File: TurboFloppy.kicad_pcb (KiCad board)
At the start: 2 copper layers, 52.1 x 66.2 mm, 10 parts, among them CN1 EXPANSION_PORT, CN3 PIN_HEADER_32PIN, U1 8255, U2 GAL20V8

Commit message: Add pull-ups on all 8255 ports
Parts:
- added RN1: 10k, Resistor_THT:R_Array_SIP9, F.Cu at (149.9, 105.9)
- added RN2: 10k, Resistor_THT:R_Array_SIP9, F.Cu at (142.2, 83.1)
- added RN3: 10k, Resistor_THT:R_Array_SIP9, F.Cu at (149.9, 83.1)
- moved CN3 3.81 mm to (165.1, 72.9)
- moved H1 3.81 mm to (123.2, 69.8)
- moved H2 3.81 mm to (168.9, 69.8)
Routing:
- net /pb3: track 35.4 -> 72.4 mm
- net /pb7: track 30.8 -> 64.1 mm
- net /pb5: track 33.3 -> 66.7 mm
- net /pb6: track 27.5 -> 60.8 mm
- net /pc4: track 18.0 -> 39.1 mm
- net /pc6: track 18.0 -> 36.0 mm
- net /pc5: track 18.0 -> 36.0 mm
- net /pc7: track 18.8 -> 36.0 mm
- net +5V: track 97.4 -> 114.5 mm
- net /pa4: track 37.9 -> 45.7 mm
- net /pa6: track 28.5 -> 36.3 mm
- net /pa5: track 33.2 -> 41.0 mm
- net /pa7: track 29.7 -> 37.4 mm
- net /d1: track 32.6 -> 37.7 mm
- net /d0: track 33.4 -> 38.3 mm
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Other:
- board size 52.1 x 66.2 mm -> 52.1 x 70 mm

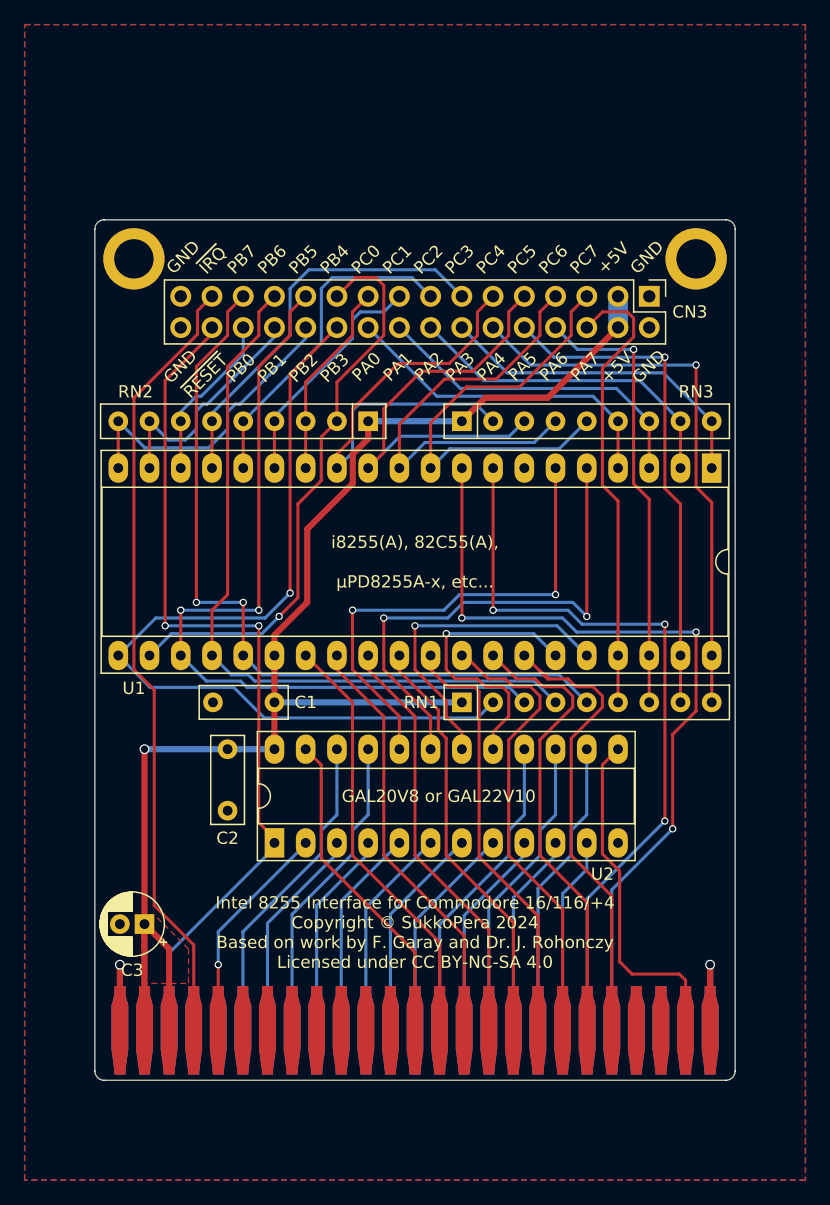
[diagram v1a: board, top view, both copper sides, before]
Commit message: Rework some tracks
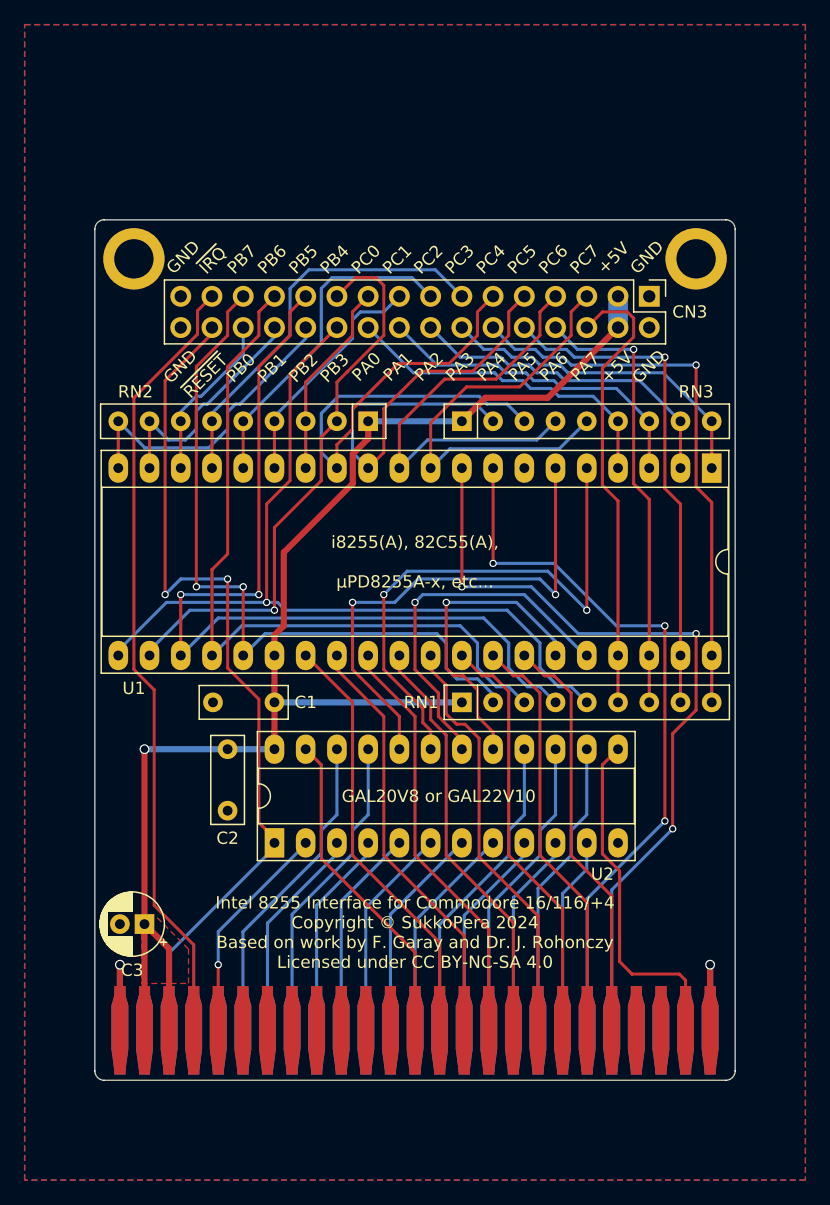
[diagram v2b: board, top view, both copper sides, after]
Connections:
- RN1 pad 2: /pb3 -> /pb7
- RN1 pad 3: /pb5 -> /pb6
- RN1 pad 4: /pb6 -> /pb5
- RN1 pad 5: /pb7 -> /pb3
- RN3 pad 2: /pc4 -> /pc5
- RN3 pad 3: /pc5 -> /pc4
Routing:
- net /pb5: track 66.7 -> 72.9 mm
- net /pc4: track 39.1 -> 44.6 mm
- net /pb7: track 64.1 -> 59.6 mm
- net /d0: track 38.3 -> 33.9 mm
- net /d1: track 37.7 -> 34.1 mm
- net /pc5: track 36.0 -> 39.2 mm
- net /~{wr8255}: track 26.6 -> 29.8 mm
- net /d2: track 37.5 -> 34.4 mm
- net /pb3: track 72.4 -> 69.4 mm
- net /~{rd8255}: track 41.8 -> 44.6 mm
- net /a1: track 61.6 -> 59.3 mm
- net /reset: track 23.5 -> 25.3 mm
- net /a0: track 66.9 -> 65.4 mm
- net /~{cs8255}: track 40.2 -> 41.6 mm
- net /d3: track 35.4 -> 34.5 mm
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
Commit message: Minor tweaks + Add URL
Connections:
- RN1 pad 5: /pb3 -> /pb4
- RN2 pad 2: /pb4 -> /pb3
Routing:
- net /pb4: track 46.7 -> 69.5 mm
- net /pb3: track 69.4 -> 50.6 mm
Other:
- board text added: "Intel 8255 Interface for Commodore 16/116/+4 Copyright © SukkoPera 2024 Based on work by F. Garay and Dr. J. Rohonczy Licensed under CC BY-NC-SA 4.0 github.com/SukkoPera/Plus4i8255"
- board text removed: "Intel 8255 Interface for Commodore 16/116/+4 Copyright © SukkoPera 2024 Based on work by F. Garay and Dr. J. Rohonczy Licensed under CC BY-NC-SA 4.0"
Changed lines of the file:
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@@
 			(layers "*.Cu" "*.Mask")
 			(remove_unused_layers no)
-			(net 60 "/pb3")
+			(net 46 "/pb4")
 			(pinfunction "R4")
 			(pintype "passive")
@@
 			(layers "*.Cu" "*.Mask")
 			(remove_unused_layers no)
-			(net 46 "/pb4")
+			(net 60 "/pb3")
 			(pinfunction "R1")
 			(pintype "passive")
@@
 		(tags "THT DIP DIL PDIP 2.54mm 7.62mm 300mil Socket LongPads")
 		(property "Reference" "U2"
-			(at -2.54 26.67 180)
+			(at 7.62 30.734 180)
 			(layer "F.SilkS")
 			(effects
@@
 		)
 	)
-	(gr_text "Intel 8255 Interface for Commodore 16/116/+4\nCopyright © SukkoPera 2024\nBased on work by F. Garay and Dr. J. Rohonczy\nLicensed under CC BY-NC-SA 4.0"
+	(gr_text "Intel 8255 Interface for Commodore 16/116/+4\nCopyright © SukkoPera 2024\nBased on work by F. Garay and Dr. J. Rohonczy\nLicensed under CC BY-NC-SA 4.0\ngithub.com/SukkoPera/Plus4i8255"
 		(at 146.05 127.635 0)
 		(layer "F.SilkS")
@@
 	)
 	(segment
-		(start 140.5255 79.0575)
-		(end 143.51 76.073)
+		(start 133.985 89.789)
+		(end 135.89 87.884)
 		(width 0.25)
 		(layer "F.Cu")
@@
 	)
 	(segment
-		(start 138.43 84.328)
-		(end 138.43 87.884)
+		(start 135.89 78.613)
+		(end 138.43 76.073)
 		(width 0.25)
 		(layer "F.Cu")
@@
 	)
 	(segment
-		(start 143.51 72.009)
-		(end 142.875 71.374)
+		(start 138.43 76.073)
+		(end 138.43 74.168)
 		(width 0.25)
 		(layer "F.Cu")
@@
 	)
 	(segment
-		(start 142.875 71.374)
-		(end 141.224 71.374)
+		(start 135.89 87.884)
+		(end 135.89 78.613)
 		(width 0.25)
 		(layer "F.Cu")
@@
 	)
 	(segment
-		(start 139.7 79.883)
-		(end 140.5255 79.0575)
+		(start 138.43 74.168)
+		(end 139.7 72.898)
 		(width 0.25)
 		(layer "F.Cu")
@@
 	)
 	(segment
-		(start 134.62 91.694)
-		(end 134.62 98.425)
+		(start 133.985 98.425)
+		(end 133.985 89.789)
 		(width 0.25)
 		(layer "F.Cu")
 		(net 46)
 	)
+	(via
+		(at 133.985 98.425)
+		(size 0.6)
+		(drill 0.4)
+		(layers "F.Cu" "B.Cu")
+		(net 46)
+	)
 	(segment
-		(start 138.43 87.884)
-		(end 134.62 91.694)
+		(start 124.46 102.108)
+		(end 124.46 101.708)
 		(width 0.25)
-		(layer "F.Cu")
+		(layer "B.Cu")
 		(net 46)
 	)
 	(segment
-		(start 139.7 83.058)
-		(end 139.7 79.883)
+		(start 156.21 103.124)
+		(end 157.734 104.648)
 		(width 0.25)
-		(layer "F.Cu")
+		(layer "B.Cu")
 		(net 46)
 	)
 	(segment
-		(start 143.51 76.073)
-		(end 143.51 72.009)
+		(start 153.543 98.425)
+		(end 156.21 101.092)
 		(width 0.25)
-		(layer "F.Cu")
+		(layer "B.Cu")
 		(net 46)
 	)
 	(segment
-		(start 139.7 83.058)
-		(end 138.43 84.328)
+		(start 156.21 101.092)
+		(end 156.21 103.124)
 		(width 0.25)
-		(layer "F.Cu")
+		(layer "B.Cu")
 		(net 46)
 	)
 	(segment
-		(start 141.224 71.374)
-		(end 139.7 72.898)
+		(start 157.734 104.648)
+		(end 158.75 104.648)
 		(width 0.25)
-		(layer "F.Cu")
+		(layer "B.Cu")
 		(net 46)
 	)
-	(via
-		(at 134.62 98.425)
-		(size 0.6)
-		(drill 0.4)
-		(layers "F.Cu" "B.Cu")
+	(segment
+		(start 127.743 98.425)
+		(end 133.985 98.425)
+		(width 0.25)
+		(layer "B.Cu")
 		(net 46)
 	)
 	(segment
-		(start 124.46 101.708)
-		(end 127.743 98.425)
+		(start 133.985 98.425)
+		(end 153.543 98.425)
 		(width 0.25)
 		(layer "B.Cu")
@@
 	)
 	(segment
-		(start 124.46 102.108)
-		(end 124.46 101.708)
+		(start 124.46 101.708)
+		(end 127.743 98.425)
 		(width 0.25)
 		(layer "B.Cu")
@@
 	)
 	(segment
-		(start 127.743 98.425)
-		(end 134.62 98.425)
+		(start 158.75 104.648)
+		(end 160.02 105.918)
 		(width 0.25)
 		(layer "B.Cu")
@@
 	)
 	(segment
-		(start 133.985 97.79)
-		(end 133.985 89.789)
+		(start 138.43 84.328)
+		(end 138.43 87.884)
 		(width 0.25)
 		(layer "F.Cu")
@@
 	)
 	(segment
-		(start 133.985 89.789)
-		(end 135.89 87.884)
+		(start 139.7 83.058)
+		(end 139.7 79.883)
 		(width 0.25)
 		(layer "F.Cu")
@@
 	)
 	(segment
-		(start 139.7 75.438)
-		(end 135.89 79.248)
+		(start 143.51 76.073)
+		(end 143.51 72.009)
 		(width 0.25)
 		(layer "F.Cu")
@@
 	)
 	(segment
-		(start 135.89 79.248)
-		(end 135.89 87.884)
+		(start 140.97 73.66)
+		(end 139.7 74.93)
 		(width 0.25)
 		(layer "F.Cu")
 		(net 60)
 	)
-	(via
-		(at 133.985 97.79)
-		(size 0.6)
-		(drill 0.4)
-		(layers "F.Cu" "B.Cu")
+	(segment
+		(start 138.43 87.884)
+		(end 134.62 91.694)
+		(width 0.25)
+		(layer "F.Cu")
 		(net 60)
 	)
 	(segment
-		(start 158.75 104.648)
-		(end 160.02 105.918)
+		(start 141.859 71.374)
+		(end 140.97 72.263)
 		(width 0.25)
-		(layer "B.Cu")
+		(layer "F.Cu")
 		(net 60)
 	)
 	(segment
-		(start 153.543 98.425)
-		(end 156.21 101.092)
+		(start 139.7 83.058)
+		(end 138.43 84.328)
 		(width 0.25)
-		(layer "B.Cu")
+		(layer "F.Cu")
 		(net 60)
 	)
 	(segment
-		(start 156.21 103.124)
-		(end 157.734 104.648)
+		(start 140.97 72.263)
+		(end 140.97 73.66)
 		(width 0.25)
-		(layer "B.Cu")
+		(layer "F.Cu")
 		(net 60)
 	)
 	(segment
-		(start 157.734 104.648)
-		(end 158.75 104.648)
+		(start 139.7 79.883)
+		(end 143.51 76.073)
 		(width 0.25)
-		(layer "B.Cu")
+		(layer "F.Cu")
 		(net 60)
 	)
 	(segment
-		(start 134.874 97.79)
-		(end 135.509 98.425)
+		(start 142.875 71.374)
+		(end 141.859 71.374)
 		(width 0.25)
-		(layer "B.Cu")
+		(layer "F.Cu")
 		(net 60)
 	)
 	(segment
-		(start 121.92 101.708)
-		(end 125.838 97.79)
+		(start 143.51 72.009)
+		(end 142.875 71.374)
 		(width 0.25)
-		(layer "B.Cu")
+		(layer "F.Cu")
 		(net 60)
 	)
 	(segment
-		(start 156.21 101.092)
-		(end 156.21 103.124)
+		(start 134.62 91.694)
+		(end 134.62 97.79)
 		(width 0.25)
-		(layer "B.Cu")
+		(layer "F.Cu")
+		(net 60)
+	)
+	(via
+		(at 134.62 97.79)
+		(size 0.6)
+		(drill 0.4)
+		(layers "F.Cu" "B.Cu")
 		(net 60)
 	)
@@
 	(segment
 		(start 125.838 97.79)
-		(end 133.985 97.79)
+		(end 134.62 97.79)
 		(width 0.25)
 		(layer "B.Cu")
@@
 	)
 	(segment
-		(start 133.985 97.79)
-		(end 134.874 97.79)
-		(width 0.25)
-		(layer "B.Cu")
-		(net 60)
-	)
-	(segment
-		(start 135.509 98.425)
-		(end 153.543 98.425)
+		(start 121.92 101.708)
+		(end 125.838 97.79)
 		(width 0.25)
 		(layer "B.Cu")
@@
 	)
 	(segment
+		(start 137.16 79.883)
+		(end 137.16 83.058)
+		(width 0.25)
+		(layer "F.Cu")
+		(net 63)
+	)
+	(segment
 		(start 137.16 86.868)
 		(end 137.16 83.058)
@@
 	(segment
 		(start 142.24 72.898)
-		(end 140.97 74.168)
+		(end 142.24 73.406)
 		(width 0.25)
 		(layer "F.Cu")
@@
 	)
 	(segment
-		(start 140.97 74.168)
+		(start 140.97 74.676)
 		(end 140.97 76.073)
 		(width 0.25)
@@
 	)
 	(segment
-		(start 140.97 76.073)
-		(end 137.16 79.883)
+		(start 142.24 73.406)
+		(end 140.97 74.676)
 		(width 0.25)
 		(layer "F.Cu")
@@
 	)
 	(segment
-		(start 137.16 79.883)
-		(end 137.16 83.058)
+		(start 140.97 76.073)
+		(end 137.16 79.883)
 		(width 0.25)
 		(layer "F.Cu")
